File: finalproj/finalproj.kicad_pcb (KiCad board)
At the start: 2 copper layers, 99.2 x 99.6 mm, 44 parts, among them J10 MotorA Out, J11 MotorB Out, J5 Stepper_Motor_Controller, J7 LIDAR_Connector, J9 RPI_UART_Conn, U1 LM1085-12, U2 LM1085-12, U3 LM1085-5.0, U4 LM1085-3.3, U5 L298N

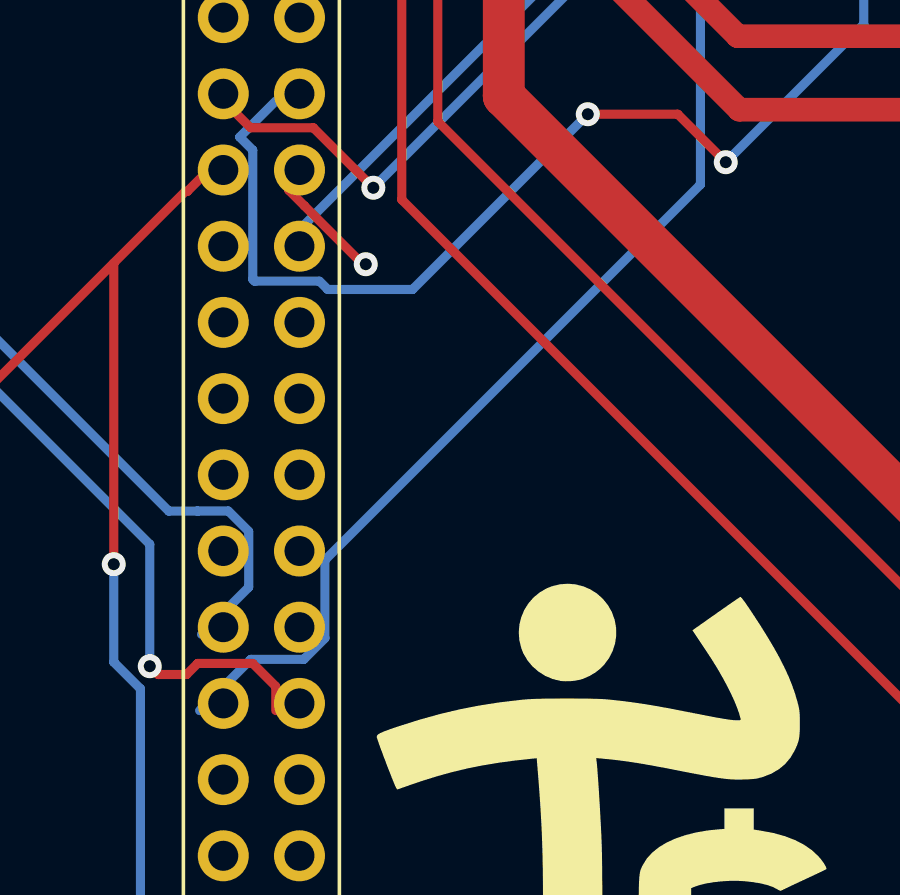
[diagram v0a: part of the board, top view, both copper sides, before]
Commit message: small try for rewiring main board headers
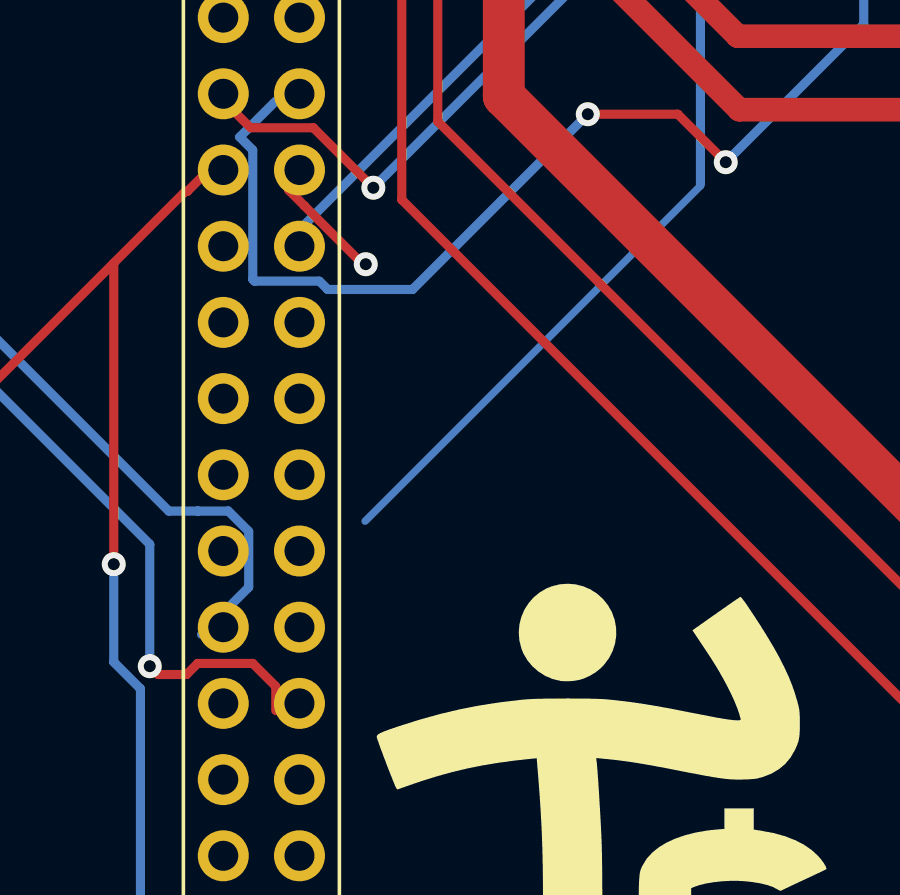
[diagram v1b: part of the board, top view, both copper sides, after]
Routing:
- net MotorAPWM: track 64.4 -> 54.8 mm
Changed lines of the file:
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@@
   (via (at 89.154102 41) (size 0.8) (drill 0.4) (layers "F.Cu" "B.Cu") (net 53))
   (via (at 78 75) (size 0.8) (drill 0.4) (layers "F.Cu" "B.Cu") (net 53))
-  (segment (start 75.933051 88.1724) (end 74.1676 88.1724) (width 0.3048) (layer "B.Cu") (net 53))
-  (segment (start 76.6374 87.468051) (end 75.933051 88.1724) (width 0.3048) (layer "B.Cu") (net 53))
   (segment (start 89.154102 41) (end 89.154602 41.0005) (width 0.3048) (layer "B.Cu") (net 53))
+  (segment (start 89.154602 72.345849) (end 89.154602 72.389398) (width 0.25) (layer "B.Cu") (net 53))
   (segment (start 89.154602 41.0005) (end 89.154602 72.345849) (width 0.3048) (layer "B.Cu") (net 53))
-  (segment (start 76.6374 84.863051) (end 76.6374 87.468051) (width 0.3048) (layer "B.Cu") (net 53))
-  (segment (start 74.1676 88.1724) (end 72.46 89.88) (width 0.3048) (layer "B.Cu") (net 53))
-  (segment (start 89.154602 72.345849) (end 76.6374 84.863051) (width 0.3048) (layer "B.Cu") (net 53))
+  (segment (start 89.154602 72.389398) (end 77.978 83.566) (width 0.25) (layer "B.Cu") (net 53))
   (segment (start 54.295 49.505) (end 54.295 50.088) (width 0.3048) (layer "B.Cu") (net 54))
   (segment (start 54.295 50.088) (end 51.651 52.732) (width 0.3048) (layer "B.Cu") (net 54))

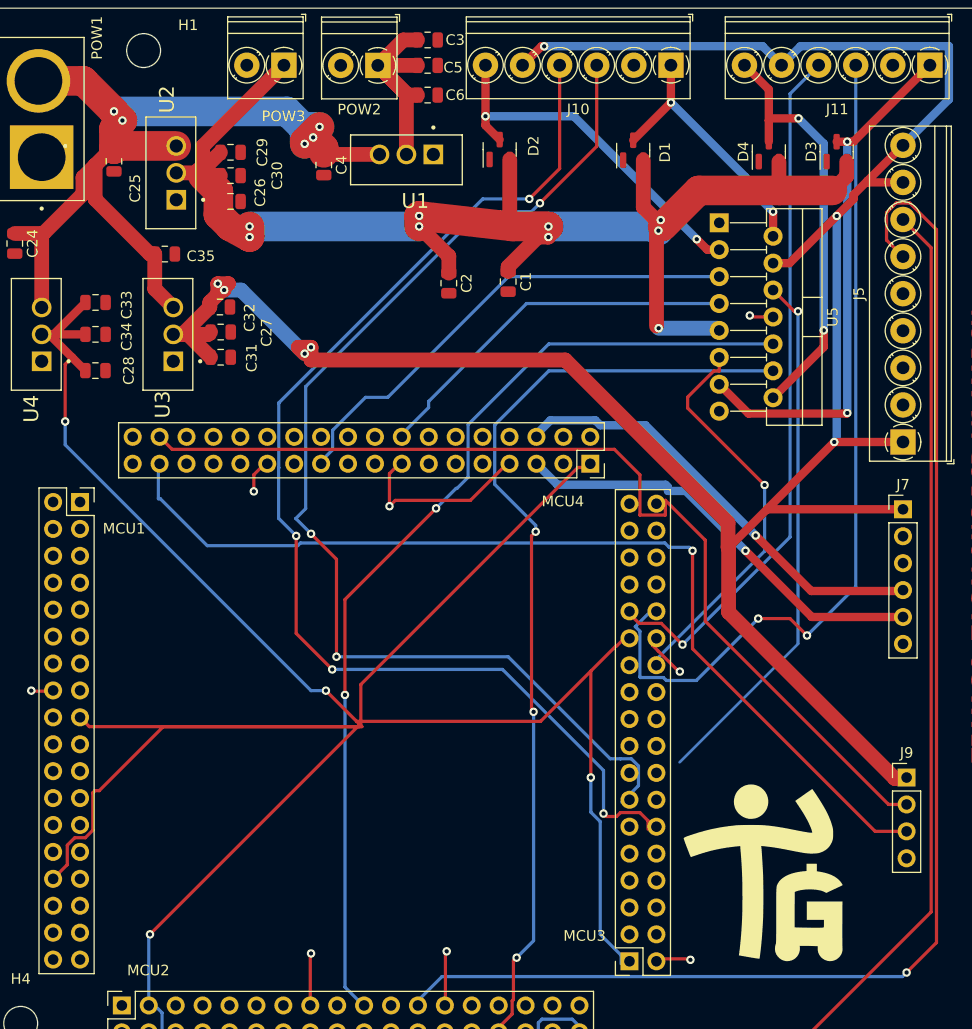
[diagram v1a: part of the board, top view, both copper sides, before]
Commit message: fixed connections on main board, weird filling and thermal errors present
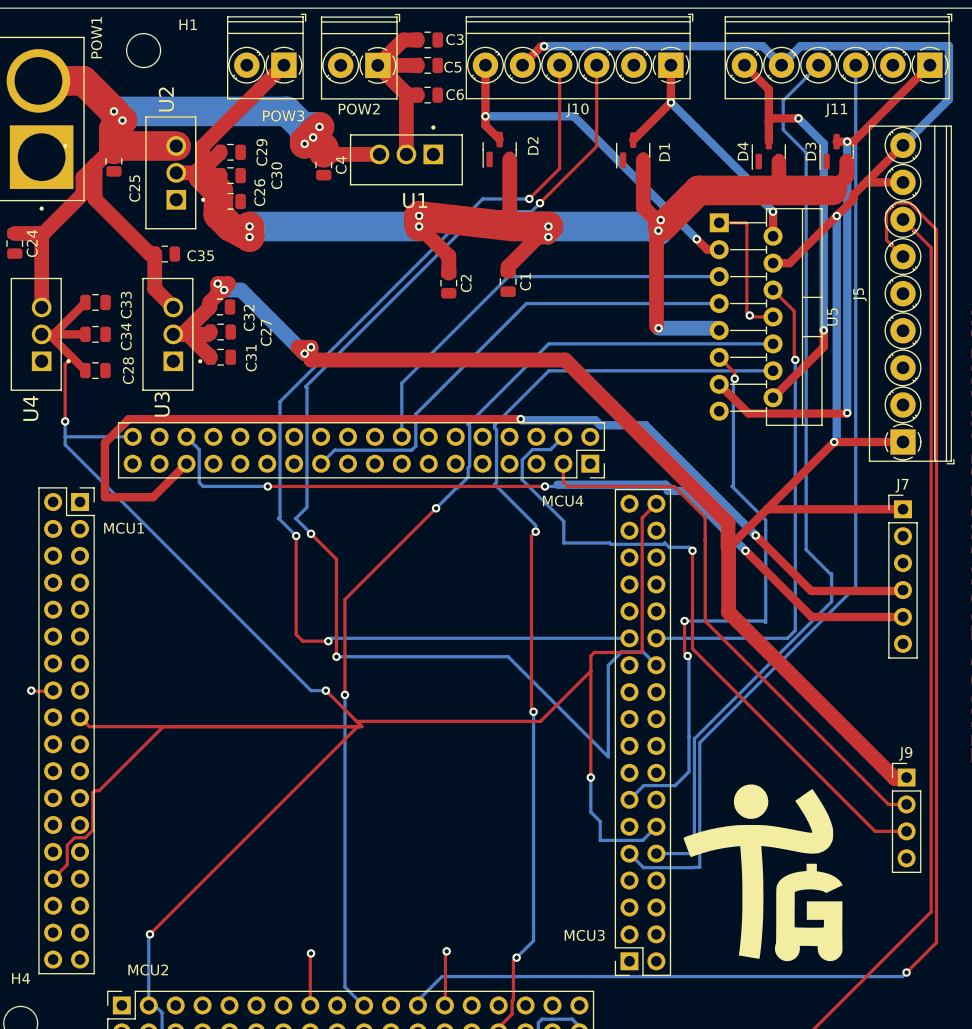
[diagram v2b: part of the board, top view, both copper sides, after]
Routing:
- net LIDAR_SCL: track 42.0 -> 97.1 mm, vias 1 -> 2
- net RPI_UART_TX: track 93.7 -> 52.4 mm
- net LIDAR_SDA: track 41.0 -> 76.8 mm, vias 1 -> 3
- net RPI_UART_RX: track 92.7 -> 63.4 mm
- net EncoderBFeedback2: track 66.7 -> 86.6 mm, vias 1 -> 0
- net MotorBPWM: track 37.8 -> 56.4 mm, vias 1 -> 3
- net VDD: track 301.2 -> 283.2 mm
- net EncoderAFeedback2: track 111.9 -> 99.8 mm, vias 4 -> 3
- net MotorAIn2: track 35.6 -> 45.6 mm
- net MotorAPWM: track 54.8 -> 46.4 mm, vias 2 -> 1
- net EncoderBFeedback1: track 81.3 -> 88.9 mm, vias 2 -> 0
- net EncoderAFeedback1: track 108.8 -> 115.9 mm
- net MotorAIn1: track 46.0 -> 39.2 mm
- net VSS: track 31.0 -> 24.9 mm, vias 5 -> 4
- net unconnected-(MCU3-PB13-Pad74): track 3.57 -> 0.00 mm, vias 1 -> 0
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
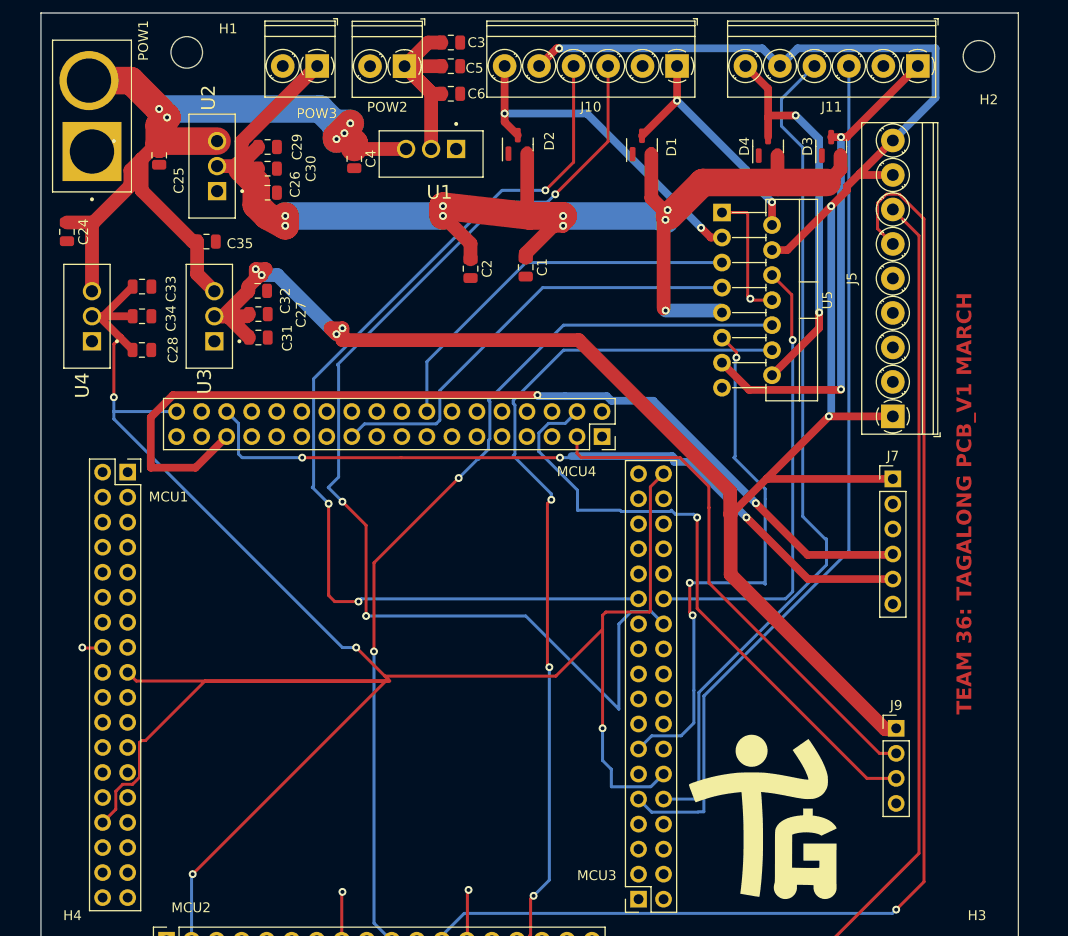
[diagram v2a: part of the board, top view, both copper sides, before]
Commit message: added resistors
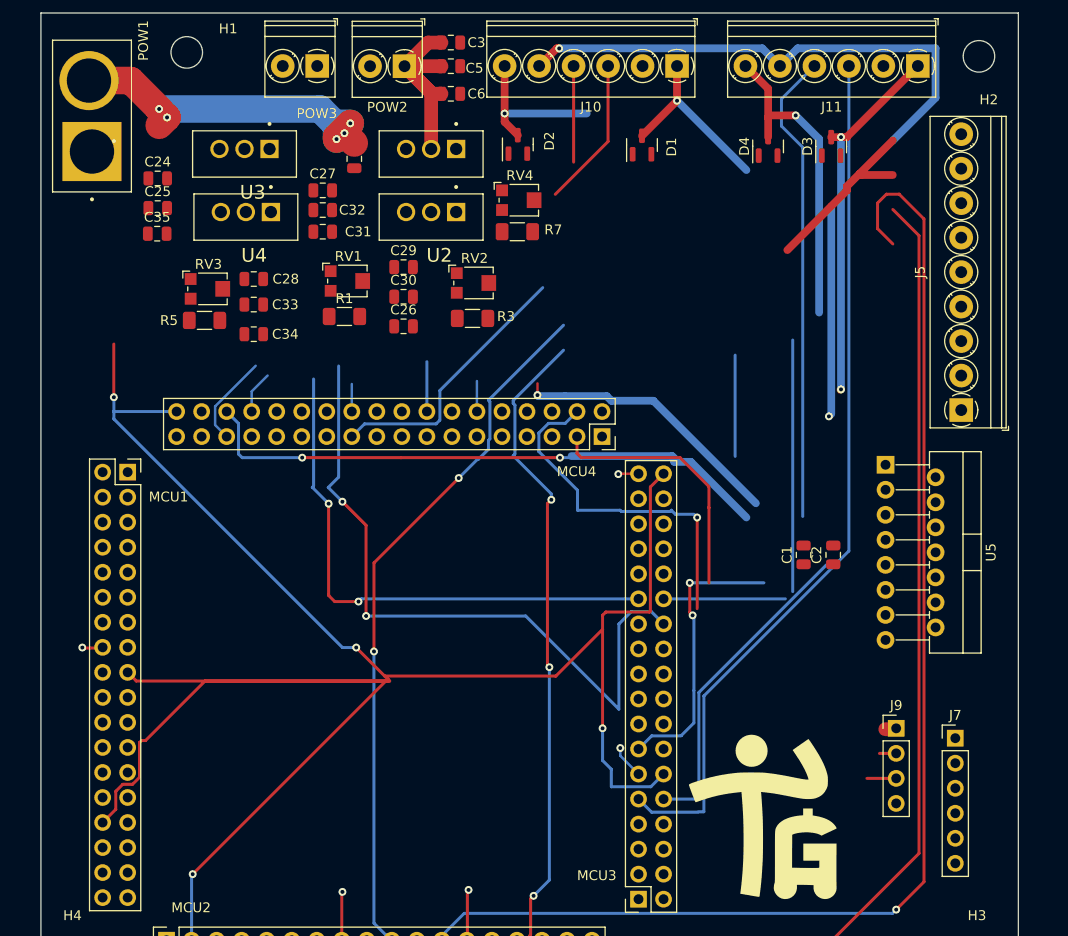
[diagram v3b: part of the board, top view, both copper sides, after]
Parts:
- added R1: 121, Resistor_SMD:R_1206_3216Metric_Pad1.30x1.75mm_HandSolder, F.Cu at (43.4, 43.2)
- added R3: 121, Resistor_SMD:R_1206_3216Metric_Pad1.30x1.75mm_HandSolder, F.Cu at (56.4, 43.4)
- added R5: 121, Resistor_SMD:R_1206_3216Metric_Pad1.30x1.75mm_HandSolder, F.Cu at (29.2, 43.6)
- added R7: 121, Resistor_SMD:R_1206_3216Metric_Pad1.30x1.75mm_HandSolder, F.Cu at (61.0, 34.6)
- added RV1: 400_Potentiometer, Potentiometer_SMD:Potentiometer_Bourns_TC33X_Vertical, F.Cu at (43.8, 39.6)
- added RV2: 1120_Potentiometer, Potentiometer_SMD:Potentiometer_Bourns_TC33X_Vertical, F.Cu at (56.6, 39.8)
- added RV3: 220_Potentiometer, Potentiometer_SMD:Potentiometer_Bourns_TC33X_Vertical, F.Cu at (29.6, 40.4)
- added RV4: 1120_Potentiometer, Potentiometer_SMD:Potentiometer_Bourns_TC33X_Vertical, F.Cu at (61.2, 31.4)
- moved C2 46.9 mm to (93.0, 67.4), turned to 90 degrees
- moved C1 40.6 mm to (90.0, 67.4), turned to 90 degrees
- moved U5 30.5 mm to (98.3, 58.2)
- moved J7 27.1 mm to (105.4, 86.0)
- moved U2 22.2 mm to (52.2, 32.6), turned to 180 degrees
- moved C26 19.3 mm to (49.4, 44.2)
- moved C30 19.0 mm to (49.4, 41.2)
- moved U4 18.9 mm to (33.4, 32.6), turned to 180 degrees
- moved C29 18.4 mm to (49.4, 38.2)
- moved U3 17.3 mm to (33.3, 26.2), turned to 180 degrees
- moved C27 14.2 mm to (41.2, 30.4)
- moved C28 13.4 mm to (34.2, 39.4)
- moved C31 12.6 mm to (41.2, 34.6)
- moved C33 11.5 mm to (34.2, 42.0)
- moved C34 11.5 mm to (34.2, 45.0)
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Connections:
- U1 pad 1: VSS -> Net-(U1-GND)
- U2 pad 1: VSS -> (no net)
- U2 pad 2: +12V -> (no net)
- U2 pad 3: BATTERY_VIN -> (no net)
- U3 pad 1: VSS -> Net-(U3-GND)
- U4 pad 1: VSS -> Net-(U4-GND)
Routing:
- net +5V: track 237.4 -> 94.5 mm, vias 7 -> 2
- net +12V: track 138.9 -> 0.00 mm, vias 9 -> 0
- net LIDAR_SCL: track 97.1 -> 37.3 mm, vias 2 -> 1
- net BATTERY_VIN: track 86.8 -> 35.9 mm
- net EncoderAFeedback2: track 99.8 -> 64.3 mm, vias 3 -> 2
- net MotorAIn1: track 39.2 -> 5.06 mm
- net EncoderAFeedback1: track 115.9 -> 86.4 mm, vias 3 -> 2
- net RPI_UART_TX: track 52.4 -> 28.0 mm
- net RPI_UART_RX: track 63.4 -> 39.0 mm
- net MotorBIn2: track 88.5 -> 67.4 mm
- net MotorBIn1: track 92.4 -> 71.2 mm
- net MotorOutA2: track 34.8 -> 15.9 mm, vias 2 -> 1
- net MotorAIn2: track 45.6 -> 27.4 mm
- net LIDAR_SDA: track 76.8 -> 59.4 mm, vias 3 -> 2
- net MotorBPWM: track 56.4 -> 38.9 mm, vias 3 -> 2
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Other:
- board text removed: "TEAM 36: TAGALONG PCB_V1 MARCH"
